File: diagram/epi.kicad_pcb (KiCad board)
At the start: 2 copper layers, 12.5 x 23 mm, 28 parts, among them J1 Conn_01x12, J2 Conn_01x12, J3 Conn_01x04, J4 USB_C_Receptacle_USB2.0, U1 ATmega32U4-M, Y1 16mhz

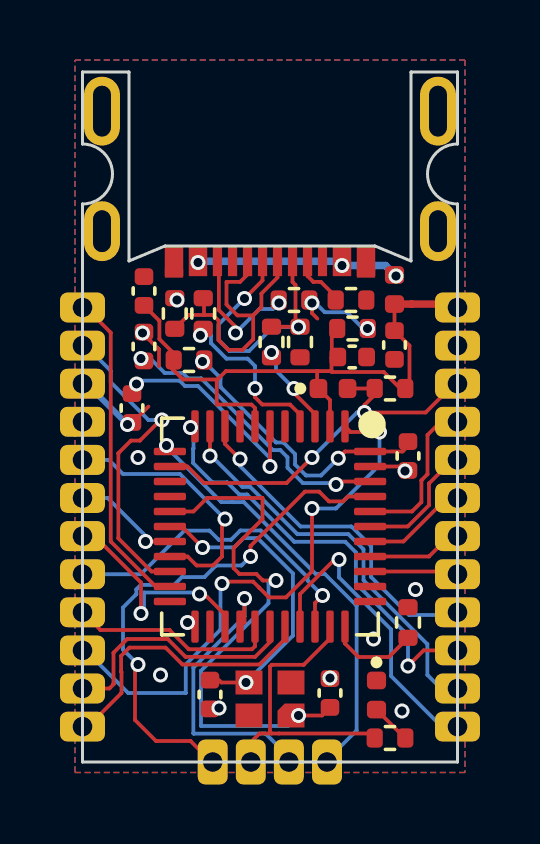
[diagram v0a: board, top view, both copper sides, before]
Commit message: redesign, added fuse
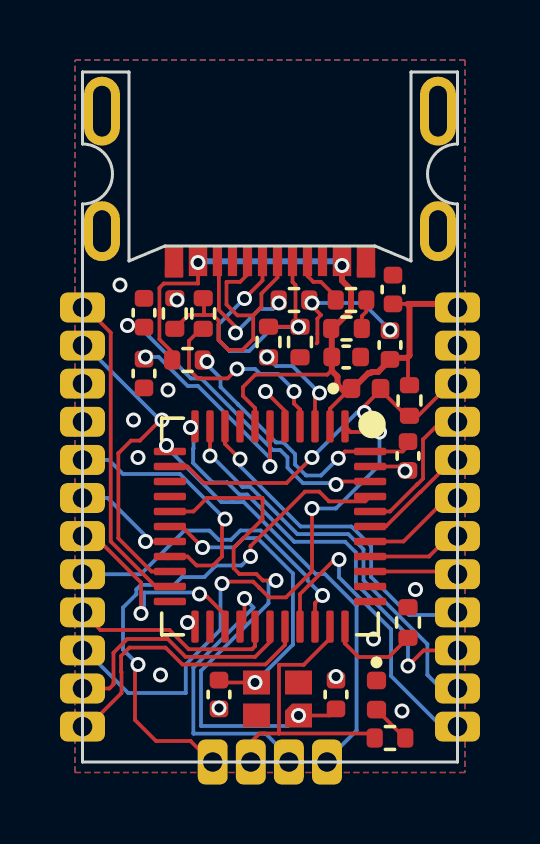
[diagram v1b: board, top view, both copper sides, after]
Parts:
- removed F1: Polyfuse_500mA, Fuse:Fuse_0402_1005Metric
- moved C3 8.30 mm to (104.1, 43.6)
- moved C8 1.22 mm to (95.8, 46.5)
- moved C7 1.12 mm to (95.8, 44.4)
- moved D1 1.10 mm to (103.2, 47.0)
- moved R6 0.76 mm to (104.7, 47.4), turned to -90 degrees
- moved C5 0.30 mm to (98.3, 57.1)
- moved Y1 0.25 mm to (100.2, 57.3)
- moved C6 0.21 mm to (102.2, 57.1)
- moved R3 0.20 mm to (102.5, 45.0)
- moved C1 0.20 mm to (102.5, 45.9)
- moved C4 0.15 mm to (104.0, 45.5), turned to 90 degrees
- moved R2 0.10 mm to (100.0, 45.4)
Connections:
- J4 pad A4: Net-(F1-Pad1) -> VBUS
- J4 pad A9: Net-(F1-Pad1) -> VBUS
- Y1 pad 3: GND -> (no net)
- Y1 pad 4: GND -> (no net)
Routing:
- net Net-(F1-Pad1): track 6.82 -> 0.00 mm, vias 3 -> 0
- net VBUS: track 22.0 -> 28.0 mm, vias 0 -> 2
- net D+: track 5.83 -> 6.86 mm
- net Net-(C7-Pad1): track 9.55 -> 10.5 mm
- net RST: track 12.9 -> 12.1 mm
- net GND: track 8.07 -> 8.31 mm, vias 14 -> 16
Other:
- board text added: "Designed and assembled in Sweden"
- board text removed: "Epi v1,1"
- board text removed: "Made in the EU"
- board text removed: "RoHS"
